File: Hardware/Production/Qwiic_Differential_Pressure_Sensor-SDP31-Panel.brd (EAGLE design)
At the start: 149.1 x 143.3 mm, 1231 parts, among them J10 QWIIC_RIGHT_ANGLE, J13 QWIIC_RIGHT_ANGLE, J14 QWIIC_RIGHT_ANGLE, J17 QWIIC_RIGHT_ANGLE, J18 QWIIC_RIGHT_ANGLE, J2 QWIIC_RIGHT_ANGLE, J21 QWIIC_RIGHT_ANGLE, J22 QWIIC_RIGHT_ANGLE, J25 QWIIC_RIGHT_ANGLE, J26 QWIIC_RIGHT_ANGLE, J29 QWIIC_RIGHT_ANGLE, J30 QWIIC_RIGHT_ANGLE, J33 QWIIC_RIGHT_ANGLE, J34 QWIIC_RIGHT_ANGLE, J37 QWIIC_RIGHT_ANGLE, J38 QWIIC_RIGHT_ANGLE, J4 QWIIC_RIGHT_ANGLE, J41 QWIIC_RIGHT_ANGLE, J42 QWIIC_RIGHT_ANGLE, J45 QWIIC_RIGHT_ANGLE, J46 QWIIC_RIGHT_ANGLE, J49 QWIIC_RIGHT_ANGLE, J5 QWIIC_RIGHT_ANGLE, J50 QWIIC_RIGHT_ANGLE, J53 QWIIC_RIGHT_ANGLE, J54 QWIIC_RIGHT_ANGLE, J57 QWIIC_RIGHT_ANGLE, J58 QWIIC_RIGHT_ANGLE, J6 QWIIC_RIGHT_ANGLE, J61 QWIIC_RIGHT_ANGLE, J62 QWIIC_RIGHT_ANGLE, J65 QWIIC_RIGHT_ANGLE, J66 QWIIC_RIGHT_ANGLE, J69 QWIIC_RIGHT_ANGLE, J70 QWIIC_RIGHT_ANGLE, J73 QWIIC_RIGHT_ANGLE, J74 QWIIC_RIGHT_ANGLE, J77 QWIIC_RIGHT_ANGLE, J78 QWIIC_RIGHT_ANGLE, J81 QWIIC_RIGHT_ANGLE, J82 QWIIC_RIGHT_ANGLE, J85 QWIIC_RIGHT_ANGLE, J86 QWIIC_RIGHT_ANGLE, J89 QWIIC_RIGHT_ANGLE, J9 QWIIC_RIGHT_ANGLE, J90 QWIIC_RIGHT_ANGLE, J93 QWIIC_RIGHT_ANGLE, J94 QWIIC_RIGHT_ANGLE, J97 QWIIC_RIGHT_ANGLE, J98 QWIIC_RIGHT_ANGLE, U1 SDP31, U10 SDP31, U11 SDP31, U12 SDP31, U13 SDP31, U14 SDP31, U15 SDP31, U16 SDP31, U17 SDP31, U18 SDP31, U19 SDP31, U2 SDP31, U20 SDP31, U21 SDP31, U22 SDP31, U23 SDP31, U24 SDP31, U25 SDP31, U3 SDP31, U4 SDP31, U5 SDP31, U6 SDP31, U7 SDP31, U8 SDP31, U9 SDP31

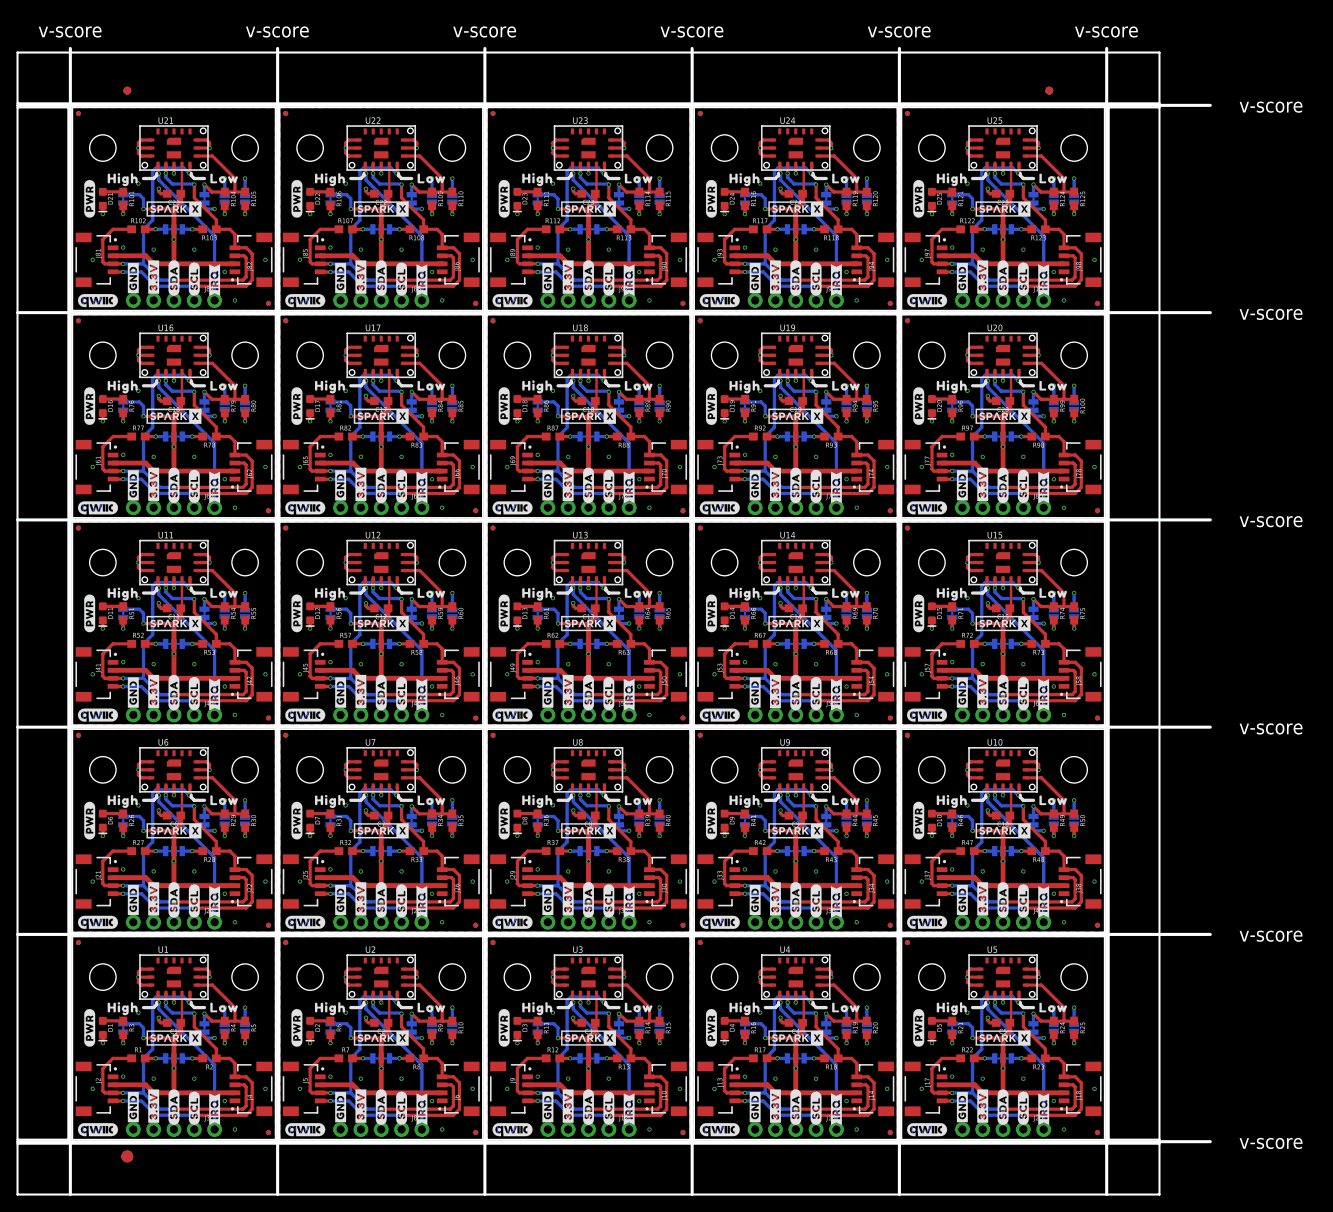
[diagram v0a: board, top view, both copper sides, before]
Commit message: Change IRQ to INT. Add Address label.
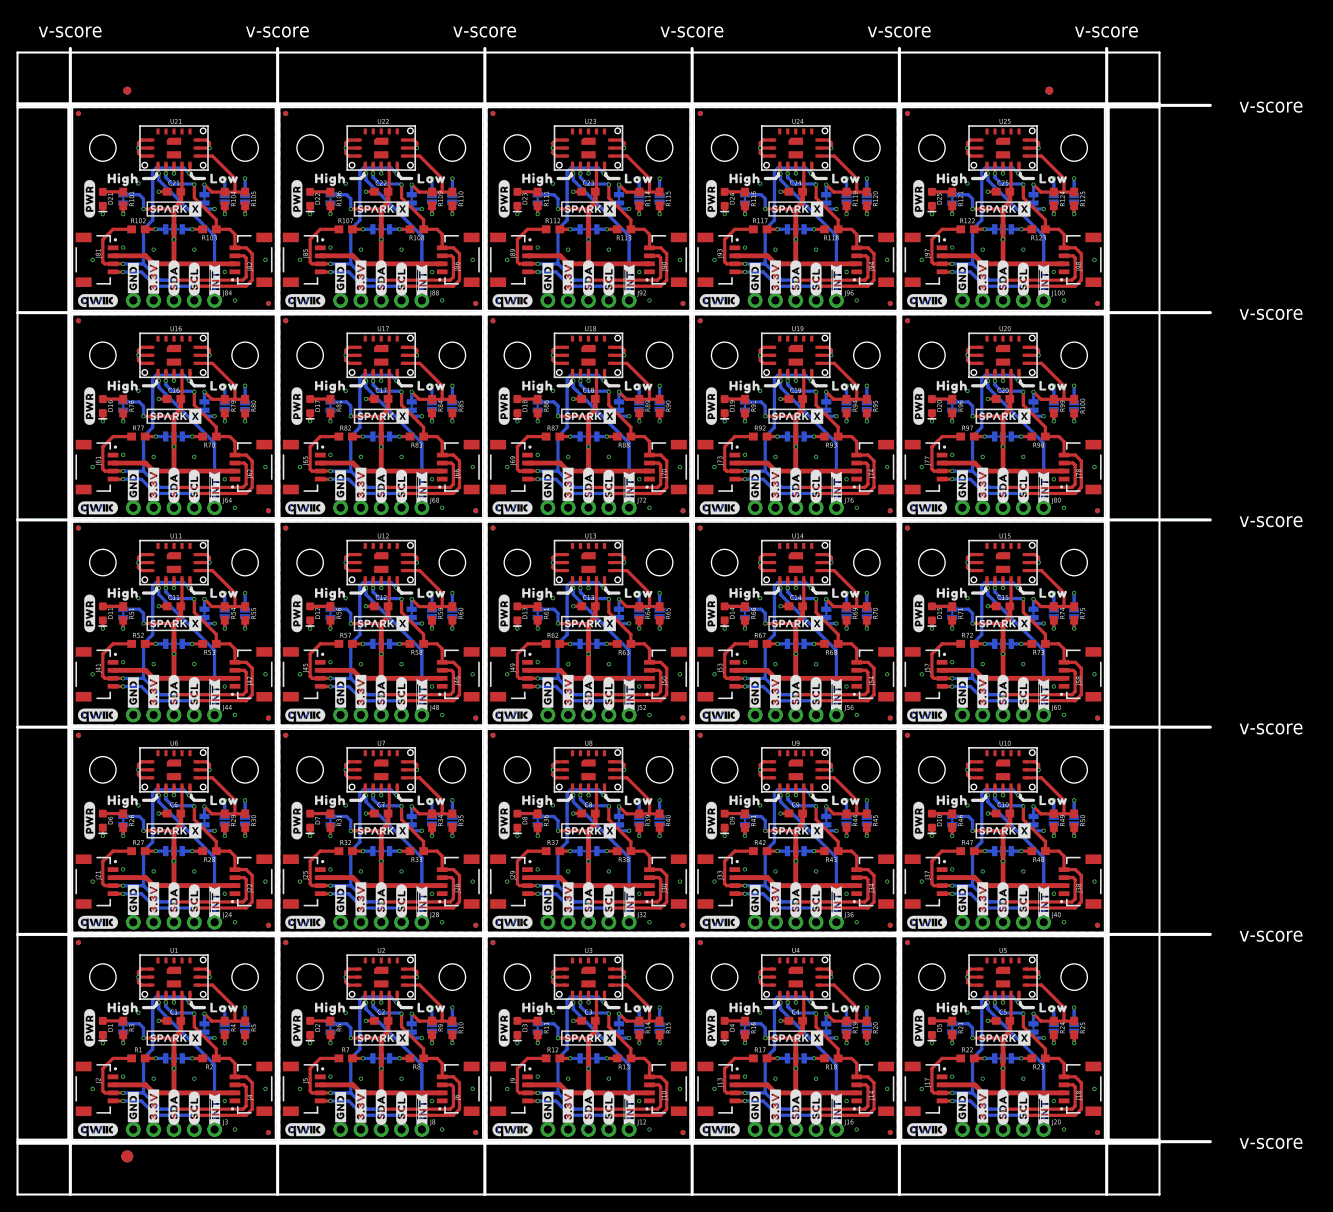
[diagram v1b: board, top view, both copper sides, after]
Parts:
- added U$626: (no value), SparkFun-Aesthetics:QWIIC_5MM
- added U$627, U$647: SPARKX-LOGO3, SparkX:SPARKX-SMALL
- added U$628: (no value), output:#PWR#0
- added U$629, U$633: (no value), output:#GND#0
- added U$630, U$634: (no value), output:#3#3V#0
- added U$631, U$635: (no value), output:#SDA#0
- added U$632, U$636: (no value), output:#SCL#0
- added U$637: (no value), output:#0X21#0
- added U$638: (no value), output:#0X22#0
- added U$639: (no value), output:#0X23#0
- added U$640: (no value), output:DIFFERENTIAL0
- added U$641: (no value), output:PRESSURE0
- added U$642: (no value), output:SENSOR0
- added U$643: (no value), output:SDP310
- added U$644: (no value), output:#LED#0
- added U$645: (no value), output:HIGH0
- added U$646: (no value), output:LOW0
- added U$648, U$649: (no value), output:##INT##0
- added U$650: (no value), output:#ADDRESS#0
- U$100, U$178: value SPARKX-LOGO3 -> (none); device SparkX:SPARKX-SMALL -> output:LOW0
- U$101, U$601: value (none) -> SPARKX-LOGO3; device SparkFun-Buzzard:I2C -> SparkX:SPARKX-SMALL
- U$102, U$77: device SparkFun-Aesthetics:QWIIC_5MM -> output:##INT##0
- U$103, U$128, U$50: value SPARKX-LOGO3 -> (none); device SparkX:SPARKX-SMALL -> output:##INT##0
- U$104: device output:#PWR#0 -> output:#ADDRESS#0
- U$105, U$209: device output:#GND#0 -> SparkFun-Buzzard:I2C
- U$106, U$210: device output:#3#3V#0 -> SparkFun-Aesthetics:QWIIC_5MM
- U$107, U$211, U$257, U$361: value (none) -> SPARKX-LOGO3; device output:#SDA#0 -> SparkX:SPARKX-SMALL
- U$108, U$212: device output:#SCL#0 -> output:#PWR#0
- U$113, U$139, U$213, U$239: device output:#IRQ#0 -> output:#GND#0
- U$114, U$188, U$214, U$88: device output:#IRQ#0 -> output:#3#3V#0
- U$115, U$215: device output:#0X21#0 -> output:#SDA#0
- U$116, U$216: device output:#0X22#0 -> output:#SCL#0
- U$117: device output:#0X23#0 -> output:#0X21#0
- U$118: device output:DIFFERENTIAL0 -> output:#0X22#0
- U$119: device output:PRESSURE0 -> output:#0X23#0
- U$120: device output:SENSOR0 -> output:DIFFERENTIAL0
- U$121: device output:SDP310 -> output:PRESSURE0
- U$122: device output:#LED#0 -> output:SENSOR0
- U$123: device output:HIGH0 -> output:SDP310
- U$124: device output:LOW0 -> output:#LED#0
- U$125, U$203: value SPARKX-LOGO3 -> (none); device SparkX:SPARKX-SMALL -> output:HIGH0
- U$126: device SparkFun-Buzzard:I2C -> output:LOW0
- U$127: value (none) -> SPARKX-LOGO3; device SparkFun-Aesthetics:QWIIC_5MM -> SparkX:SPARKX-SMALL
- U$129, U$154: device output:#PWR#0 -> output:##INT##0
- U$130, U$234: device output:#GND#0 -> output:#ADDRESS#0
- U$131, U$235: device output:#3#3V#0 -> SparkFun-Buzzard:I2C
- U$132, U$236: device output:#SDA#0 -> SparkFun-Aesthetics:QWIIC_5MM
- U$133, U$237, U$283, U$387: value (none) -> SPARKX-LOGO3; device output:#SCL#0 -> SparkX:SPARKX-SMALL
- U$134, U$25: device output:#GND#0 -> output:#PWR#0
- U$135, U$26, U$30, U$581: device output:#3#3V#0 -> output:#GND#0
- U$136, U$27, U$31, U$582: device output:#SDA#0 -> output:#3#3V#0
- U$137, U$28, U$37, U$583: device output:#SCL#0 -> output:#SDA#0
- U$138, U$164, U$38, U$64: device output:#IRQ#0 -> output:#SCL#0
- U$140, U$240: device output:#0X21#0 -> output:#3#3V#0
- U$141, U$241: device output:#0X22#0 -> output:#SDA#0
- U$142, U$242: device output:#0X23#0 -> output:#SCL#0
- U$143: device output:DIFFERENTIAL0 -> output:#0X21#0
- U$144: device output:PRESSURE0 -> output:#0X22#0
- U$145: device output:SENSOR0 -> output:#0X23#0
- U$146: device output:SDP310 -> output:DIFFERENTIAL0
- U$147: device output:#LED#0 -> output:PRESSURE0
- U$148: device output:HIGH0 -> output:SENSOR0
- U$149: device output:LOW0 -> output:SDP310
- U$150, U$228: value SPARKX-LOGO3 -> (none); device SparkX:SPARKX-SMALL -> output:#LED#0
- U$151: device SparkFun-Buzzard:I2C -> output:HIGH0
- U$152: device SparkFun-Aesthetics:QWIIC_5MM -> output:LOW0
- U$155, U$180, U$259, U$284: device output:#GND#0 -> output:##INT##0
- U$156, U$260: device output:#3#3V#0 -> output:#ADDRESS#0
- U$157, U$261: device output:#SDA#0 -> SparkFun-Buzzard:I2C
- U$158, U$262: device output:#SCL#0 -> SparkFun-Aesthetics:QWIIC_5MM
- U$159, U$205, U$309, U$55: value (none) -> SPARKX-LOGO3; device output:#GND#0 -> SparkX:SPARKX-SMALL
- U$160, U$56: device output:#3#3V#0 -> output:#PWR#0
- U$161, U$57, U$607, U$61: device output:#SDA#0 -> output:#GND#0
- U$162, U$58, U$608, U$62: device output:#SCL#0 -> output:#3#3V#0
- U$163, U$189, U$63, U$89: device output:#IRQ#0 -> output:#SDA#0
- U$165, U$265: device output:#0X21#0 -> output:#GND#0
- U$166, U$266: device output:#0X22#0 -> output:#3#3V#0
- U$167, U$267: device output:#0X23#0 -> output:#SDA#0
- U$168, U$268: device output:DIFFERENTIAL0 -> output:#SCL#0
- U$169: device output:PRESSURE0 -> output:#0X21#0
- U$170: device output:SENSOR0 -> output:#0X22#0
- U$171: device output:SDP310 -> output:#0X23#0
- U$172: device output:#LED#0 -> output:DIFFERENTIAL0
- U$173: device output:HIGH0 -> output:PRESSURE0
- U$174: device output:LOW0 -> output:SENSOR0
- U$175, U$253: value SPARKX-LOGO3 -> (none); device SparkX:SPARKX-SMALL -> output:SDP310
- U$176: device SparkFun-Buzzard:I2C -> output:#LED#0
- U$177: device SparkFun-Aesthetics:QWIIC_5MM -> output:HIGH0
- U$179, U$24: value (none) -> SPARKX-LOGO3; device output:#PWR#0 -> SparkX:SPARKX-SMALL
- U$181, U$206, U$285, U$310: device output:#3#3V#0 -> output:##INT##0
- U$182, U$286: device output:#SDA#0 -> output:#ADDRESS#0
- U$183, U$287: device output:#SCL#0 -> SparkFun-Buzzard:I2C
- U$184, U$80: device output:#GND#0 -> SparkFun-Aesthetics:QWIIC_5MM
- U$185, U$231, U$335, U$81: value (none) -> SPARKX-LOGO3; device output:#3#3V#0 -> SparkX:SPARKX-SMALL
- U$186, U$82: device output:#SDA#0 -> output:#PWR#0
- U$187, U$83, U$87: device output:#SCL#0 -> output:#GND#0
- U$190, U$90: device output:#0X21#0 -> output:#SCL#0
- U$191, U$291: device output:#0X22#0 -> output:#GND#0
- U$192, U$292: device output:#0X23#0 -> output:#3#3V#0
- U$193, U$293: device output:DIFFERENTIAL0 -> output:#SDA#0
- U$194, U$294: device output:PRESSURE0 -> output:#SCL#0
- U$195: device output:SENSOR0 -> output:#0X21#0
- U$196: device output:SDP310 -> output:#0X22#0
- U$197: device output:#LED#0 -> output:#0X23#0
- U$198: device output:HIGH0 -> output:DIFFERENTIAL0
- U$199: device output:LOW0 -> output:PRESSURE0
- U$200, U$278: value SPARKX-LOGO3 -> (none); device SparkX:SPARKX-SMALL -> output:SENSOR0
- U$201: device SparkFun-Buzzard:I2C -> output:SDP310
- U$202: device SparkFun-Aesthetics:QWIIC_5MM -> output:#LED#0
- U$204: device output:#PWR#0 -> output:LOW0
- U$207, U$232, U$311, U$336: device output:#SDA#0 -> output:##INT##0
- U$208, U$312: device output:#SCL#0 -> output:#ADDRESS#0
- U$21: device SparkFun-Buzzard:I2C -> output:#ADDRESS#0
- U$217, U$317: device output:#0X23#0 -> output:#GND#0
- U$218, U$318: device output:DIFFERENTIAL0 -> output:#3#3V#0
- U$219, U$319: device output:PRESSURE0 -> output:#SDA#0
- U$22: device SparkFun-Aesthetics:QWIIC_5MM -> SparkFun-Buzzard:I2C
- U$220, U$320: device output:SENSOR0 -> output:#SCL#0
- U$221: device output:SDP310 -> output:#0X21#0
- U$222: device output:#LED#0 -> output:#0X22#0
- U$223: device output:HIGH0 -> output:#0X23#0
- U$224: device output:LOW0 -> output:DIFFERENTIAL0
- U$225, U$303: value SPARKX-LOGO3 -> (none); device SparkX:SPARKX-SMALL -> output:PRESSURE0
- U$226: device SparkFun-Buzzard:I2C -> output:SENSOR0
- U$227: device SparkFun-Aesthetics:QWIIC_5MM -> output:SDP310
- U$229: device output:#PWR#0 -> output:HIGH0
- U$23, U$600: value SPARKX-LOGO3 -> (none); device SparkX:SPARKX-SMALL -> SparkFun-Aesthetics:QWIIC_5MM
- U$230, U$334: device output:#GND#0 -> output:LOW0
- U$233, U$258, U$337, U$362: device output:#SCL#0 -> output:##INT##0
- U$238, U$264: device output:#IRQ#0 -> output:#PWR#0
- U$243, U$343: device output:DIFFERENTIAL0 -> output:#GND#0
- U$244, U$344: device output:PRESSURE0 -> output:#3#3V#0
- U$245, U$345: device output:SENSOR0 -> output:#SDA#0
- U$246, U$346: device output:SDP310 -> output:#SCL#0
- U$247: device output:#LED#0 -> output:#0X21#0
- U$248: device output:HIGH0 -> output:#0X22#0
- U$249: device output:LOW0 -> output:#0X23#0
- U$250, U$328: value SPARKX-LOGO3 -> (none); device SparkX:SPARKX-SMALL -> output:DIFFERENTIAL0
- U$251: device SparkFun-Buzzard:I2C -> output:PRESSURE0
- U$252: device SparkFun-Aesthetics:QWIIC_5MM -> output:SENSOR0
- U$254: device output:#PWR#0 -> output:#LED#0
- U$255, U$359: device output:#GND#0 -> output:HIGH0
- U$256, U$360: device output:#3#3V#0 -> output:LOW0
- U$263, U$289, U$413, U$439: value (none) -> SPARKX-LOGO3; device output:#IRQ#0 -> SparkX:SPARKX-SMALL
- U$269, U$369: device output:PRESSURE0 -> output:#GND#0
- U$270, U$370: device output:SENSOR0 -> output:#3#3V#0
- U$271, U$371: device output:SDP310 -> output:#SDA#0
- U$272, U$372: device output:#LED#0 -> output:#SCL#0
- U$273: device output:HIGH0 -> output:#0X21#0
- U$274: device output:LOW0 -> output:#0X22#0
- U$275, U$353: value SPARKX-LOGO3 -> (none); device SparkX:SPARKX-SMALL -> output:#0X23#0
- U$276: device SparkFun-Buzzard:I2C -> output:DIFFERENTIAL0
- U$277: device SparkFun-Aesthetics:QWIIC_5MM -> output:PRESSURE0
- U$279: device output:#PWR#0 -> output:SDP310
- U$280, U$384: device output:#GND#0 -> output:#LED#0
- U$281, U$385: device output:#3#3V#0 -> output:HIGH0
- U$282, U$386: device output:#SDA#0 -> output:LOW0
- U$288, U$314: device output:#IRQ#0 -> SparkFun-Aesthetics:QWIIC_5MM
- U$29, U$480, U$580, U$584: device output:#GND#0 -> output:#SCL#0
- U$290: device output:#0X21#0 -> output:#PWR#0
- U$295, U$395: device output:SENSOR0 -> output:#GND#0
- U$296, U$396: device output:SDP310 -> output:#3#3V#0
- U$297, U$397: device output:#LED#0 -> output:#SDA#0
- U$298, U$398: device output:HIGH0 -> output:#SCL#0
- U$299: device output:LOW0 -> output:#0X21#0
- U$300, U$378: value SPARKX-LOGO3 -> (none); device SparkX:SPARKX-SMALL -> output:#0X22#0
- U$301: device SparkFun-Buzzard:I2C -> output:#0X23#0
- U$302: device SparkFun-Aesthetics:QWIIC_5MM -> output:DIFFERENTIAL0
- U$304: device output:#PWR#0 -> output:SENSOR0
- U$305, U$409: device output:#GND#0 -> output:SDP310
- U$306, U$410: device output:#3#3V#0 -> output:#LED#0
- U$307, U$411: device output:#SDA#0 -> output:HIGH0
- U$308, U$412: device output:#SCL#0 -> output:LOW0
- U$313, U$339: device output:#IRQ#0 -> SparkFun-Buzzard:I2C
- U$315, U$465: value (none) -> SPARKX-LOGO3; device output:#0X21#0 -> SparkX:SPARKX-SMALL
- U$316: device output:#0X22#0 -> output:#PWR#0
- U$321, U$421: device output:SDP310 -> output:#GND#0
- U$322, U$422: device output:#LED#0 -> output:#3#3V#0
- U$323, U$423: device output:HIGH0 -> output:#SDA#0
- U$324, U$424: device output:LOW0 -> output:#SCL#0
- U$325, U$403: value SPARKX-LOGO3 -> (none); device SparkX:SPARKX-SMALL -> output:#0X21#0
- U$326: device SparkFun-Buzzard:I2C -> output:#0X22#0
- U$327: device SparkFun-Aesthetics:QWIIC_5MM -> output:#0X23#0
- U$329: device output:#PWR#0 -> output:PRESSURE0
- U$330, U$434: device output:#GND#0 -> output:SENSOR0
- U$331, U$435: device output:#3#3V#0 -> output:SDP310
- U$332, U$436: device output:#SDA#0 -> output:#LED#0
- U$333, U$437: device output:#SCL#0 -> output:HIGH0
- U$338, U$364: device output:#IRQ#0 -> output:#ADDRESS#0
- U$340: device output:#0X21#0 -> SparkFun-Aesthetics:QWIIC_5MM
- U$341, U$491: value (none) -> SPARKX-LOGO3; device output:#0X22#0 -> SparkX:SPARKX-SMALL
- U$342: device output:#0X23#0 -> output:#PWR#0
- U$347, U$447: device output:#LED#0 -> output:#GND#0
- U$348, U$448: device output:HIGH0 -> output:#3#3V#0
- U$349, U$449: device output:LOW0 -> output:#SDA#0
- U$350, U$428, U$450, U$528: value SPARKX-LOGO3 -> (none); device SparkX:SPARKX-SMALL -> output:#SCL#0
- U$351: device SparkFun-Buzzard:I2C -> output:#0X21#0
- U$352: device SparkFun-Aesthetics:QWIIC_5MM -> output:#0X22#0
- U$354: device output:#PWR#0 -> output:DIFFERENTIAL0
- U$355, U$459: device output:#GND#0 -> output:PRESSURE0
- U$356, U$460: device output:#3#3V#0 -> output:SENSOR0
- U$357, U$461: device output:#SDA#0 -> output:SDP310
- U$358, U$462: device output:#SCL#0 -> output:#LED#0
- U$363, U$388, U$389, U$414, U$5, U$6: device output:#IRQ#0 -> output:##INT##0
- U$365: device output:#0X21#0 -> SparkFun-Buzzard:I2C
- U$366: device output:#0X22#0 -> SparkFun-Aesthetics:QWIIC_5MM
- U$367, U$517: value (none) -> SPARKX-LOGO3; device output:#0X23#0 -> SparkX:SPARKX-SMALL
- U$368: device output:DIFFERENTIAL0 -> output:#PWR#0
- U$373, U$473: device output:HIGH0 -> output:#GND#0
- U$374, U$474: device output:LOW0 -> output:#3#3V#0
- U$375, U$453, U$475, U$553: value SPARKX-LOGO3 -> (none); device SparkX:SPARKX-SMALL -> output:#SDA#0
- U$376, U$476: device SparkFun-Buzzard:I2C -> output:#SCL#0
- U$377: device SparkFun-Aesthetics:QWIIC_5MM -> output:#0X21#0
- U$379: device output:#PWR#0 -> output:#0X23#0
- U$380, U$484: device output:#GND#0 -> output:DIFFERENTIAL0
- U$381, U$485: device output:#3#3V#0 -> output:PRESSURE0
- U$382, U$486: device output:#SDA#0 -> output:SENSOR0
- U$383, U$487: device output:#SCL#0 -> output:SDP310
- U$39: device output:#IRQ#0 -> output:#0X21#0
- U$390: device output:#0X21#0 -> output:#ADDRESS#0
- U$391: device output:#0X22#0 -> SparkFun-Buzzard:I2C
- U$392: device output:#0X23#0 -> SparkFun-Aesthetics:QWIIC_5MM
- U$393, U$543: value (none) -> SPARKX-LOGO3; device output:DIFFERENTIAL0 -> SparkX:SPARKX-SMALL
- U$394: device output:PRESSURE0 -> output:#PWR#0
- U$399, U$499: device output:LOW0 -> output:#GND#0
- U$40: device output:#0X21#0 -> output:#0X22#0
- U$400, U$478, U$500, U$578: value SPARKX-LOGO3 -> (none); device SparkX:SPARKX-SMALL -> output:#3#3V#0
- U$401, U$501: device SparkFun-Buzzard:I2C -> output:#SDA#0
- U$402, U$502: device SparkFun-Aesthetics:QWIIC_5MM -> output:#SCL#0
- U$404: device output:#PWR#0 -> output:#0X22#0
- U$405, U$509: device output:#GND#0 -> output:#0X23#0
- U$406, U$510: device output:#3#3V#0 -> output:DIFFERENTIAL0
- U$407, U$511: device output:#SDA#0 -> output:PRESSURE0
- U$408, U$512: device output:#SCL#0 -> output:SENSOR0
- U$41: device output:#0X22#0 -> output:#0X23#0
- U$415, U$440: device output:#0X21#0 -> output:##INT##0
- U$416: device output:#0X22#0 -> output:#ADDRESS#0
- U$417: device output:#0X23#0 -> SparkFun-Buzzard:I2C
- U$418: device output:DIFFERENTIAL0 -> SparkFun-Aesthetics:QWIIC_5MM
- U$419, U$569: value (none) -> SPARKX-LOGO3; device output:PRESSURE0 -> SparkX:SPARKX-SMALL
- U$42: device output:#0X23#0 -> output:DIFFERENTIAL0
- U$420: device output:SENSOR0 -> output:#PWR#0
- U$425, U$503, U$525, U$603: value SPARKX-LOGO3 -> (none); device SparkX:SPARKX-SMALL -> output:#GND#0
- U$426, U$526: device SparkFun-Buzzard:I2C -> output:#3#3V#0
- U$427, U$527: device SparkFun-Aesthetics:QWIIC_5MM -> output:#SDA#0
- U$429: device output:#PWR#0 -> output:#0X21#0
- U$43: device output:DIFFERENTIAL0 -> output:PRESSURE0
- U$430, U$534: device output:#GND#0 -> output:#0X22#0
- U$431, U$535: device output:#3#3V#0 -> output:#0X23#0
- U$432, U$536: device output:#SDA#0 -> output:DIFFERENTIAL0
- U$433, U$537: device output:#SCL#0 -> output:PRESSURE0
- U$438, U$464: device output:#IRQ#0 -> output:LOW0
- U$44: device output:PRESSURE0 -> output:SENSOR0
- U$441, U$466: device output:#0X22#0 -> output:##INT##0
- U$442: device output:#0X23#0 -> output:#ADDRESS#0
- U$443: device output:DIFFERENTIAL0 -> SparkFun-Buzzard:I2C
- U$444: device output:PRESSURE0 -> SparkFun-Aesthetics:QWIIC_5MM
- U$445, U$595: value (none) -> SPARKX-LOGO3; device output:SENSOR0 -> SparkX:SPARKX-SMALL
- U$446: device output:SDP310 -> output:#PWR#0
- U$45: device output:SENSOR0 -> output:SDP310
- U$451, U$551: device SparkFun-Buzzard:I2C -> output:#GND#0
- U$452, U$552: device SparkFun-Aesthetics:QWIIC_5MM -> output:#3#3V#0
- U$454, U$554: device output:#PWR#0 -> output:#SCL#0
- U$455, U$559: device output:#GND#0 -> output:#0X21#0
- U$456, U$560: device output:#3#3V#0 -> output:#0X22#0
- U$457, U$561: device output:#SDA#0 -> output:#0X23#0
- U$458, U$562: device output:#SCL#0 -> output:DIFFERENTIAL0
- U$46: device output:SDP310 -> output:#LED#0
- U$463, U$489: device output:#IRQ#0 -> output:HIGH0
- U$467, U$492: device output:#0X23#0 -> output:##INT##0
- U$468: device output:DIFFERENTIAL0 -> output:#ADDRESS#0
- U$469: device output:PRESSURE0 -> SparkFun-Buzzard:I2C
- U$47: device output:#LED#0 -> output:HIGH0
- U$470: device output:SENSOR0 -> SparkFun-Aesthetics:QWIIC_5MM
- U$471, U$621: value (none) -> SPARKX-LOGO3; device output:SDP310 -> SparkX:SPARKX-SMALL
- U$472: device output:#LED#0 -> output:#PWR#0
- U$477, U$577: device SparkFun-Aesthetics:QWIIC_5MM -> output:#GND#0
- U$479, U$579: device output:#PWR#0 -> output:#SDA#0
- U$48: device output:HIGH0 -> output:LOW0
- U$481, U$585: device output:#3#3V#0 -> output:#0X21#0
- U$482, U$586: device output:#SDA#0 -> output:#0X22#0
- U$483, U$587: device output:#SCL#0 -> output:#0X23#0
- U$488, U$514: device output:#IRQ#0 -> output:#LED#0
- U$49, U$549: value (none) -> SPARKX-LOGO3; device output:LOW0 -> SparkX:SPARKX-SMALL
- U$490: device output:#0X21#0 -> output:LOW0
- U$493, U$518: device output:DIFFERENTIAL0 -> output:##INT##0
- U$494: device output:PRESSURE0 -> output:#ADDRESS#0
- U$495: device output:SENSOR0 -> SparkFun-Buzzard:I2C
- U$496: device output:SDP310 -> SparkFun-Aesthetics:QWIIC_5MM
- U$497: value (none) -> SPARKX-LOGO3; device output:#LED#0 -> SparkX:SPARKX-SMALL
- U$498: device output:HIGH0 -> output:#PWR#0
- U$504, U$604: device output:#PWR#0 -> output:#3#3V#0
- U$505, U$59, U$605, U$609: device output:#GND#0 -> output:#SDA#0
- U$506, U$60, U$606, U$610: device output:#3#3V#0 -> output:#SCL#0
- U$507, U$611: device output:#SDA#0 -> output:#0X21#0
- U$508, U$612: device output:#SCL#0 -> output:#0X22#0
- U$51, U$76: device SparkFun-Buzzard:I2C -> output:##INT##0
- U$513, U$539: device output:#IRQ#0 -> output:SDP310
- U$515: device output:#0X21#0 -> output:HIGH0
- U$516: device output:#0X22#0 -> output:LOW0
- U$519, U$544: device output:PRESSURE0 -> output:##INT##0
- U$52: device SparkFun-Aesthetics:QWIIC_5MM -> output:#ADDRESS#0
- U$520: device output:SENSOR0 -> output:#ADDRESS#0
- U$521: device output:SDP310 -> SparkFun-Buzzard:I2C
- U$522: device output:#LED#0 -> SparkFun-Aesthetics:QWIIC_5MM
- U$523: value (none) -> SPARKX-LOGO3; device output:HIGH0 -> SparkX:SPARKX-SMALL
- U$524: device output:LOW0 -> output:#PWR#0
- U$529: device output:#PWR#0 -> output:#GND#0
- U$53, U$625: value SPARKX-LOGO3 -> (none); device SparkX:SPARKX-SMALL -> SparkFun-Buzzard:I2C
- U$530, U$84: device output:#GND#0 -> output:#3#3V#0
- U$531, U$85: device output:#3#3V#0 -> output:#SDA#0
- U$532, U$86: device output:#SDA#0 -> output:#SCL#0
- U$533: device output:#SCL#0 -> output:#0X21#0
- U$538, U$564: device output:#IRQ#0 -> output:SENSOR0
- U$54: device output:#PWR#0 -> SparkFun-Aesthetics:QWIIC_5MM
- U$540: device output:#0X21#0 -> output:#LED#0
- U$541: device output:#0X22#0 -> output:HIGH0
- U$542: device output:#0X23#0 -> output:LOW0
- U$545, U$570: device output:SENSOR0 -> output:##INT##0
- U$546: device output:SDP310 -> output:#ADDRESS#0
- U$547: device output:#LED#0 -> SparkFun-Buzzard:I2C
- U$548: device output:HIGH0 -> SparkFun-Aesthetics:QWIIC_5MM
- U$550: value SPARKX-LOGO3 -> (none); device SparkX:SPARKX-SMALL -> output:#PWR#0
- U$563, U$589: device output:#IRQ#0 -> output:PRESSURE0
- U$565: device output:#0X21#0 -> output:SDP310
- U$566: device output:#0X22#0 -> output:#LED#0
- U$567: device output:#0X23#0 -> output:HIGH0
- U$568: device output:DIFFERENTIAL0 -> output:LOW0
- U$571, U$596: device output:SDP310 -> output:##INT##0
- U$572: device output:#LED#0 -> output:#ADDRESS#0
- U$573: device output:HIGH0 -> SparkFun-Buzzard:I2C
- U$574: device output:LOW0 -> SparkFun-Aesthetics:QWIIC_5MM
- U$576: device SparkFun-Buzzard:I2C -> output:#PWR#0
- U$588, U$614: device output:#IRQ#0 -> output:DIFFERENTIAL0
- U$590: device output:#0X21#0 -> output:SENSOR0
- U$591: device output:#0X22#0 -> output:SDP310
- U$592: device output:#0X23#0 -> output:#LED#0
- U$593: device output:DIFFERENTIAL0 -> output:HIGH0
- U$594: device output:PRESSURE0 -> output:LOW0
- U$597, U$622: device output:#LED#0 -> output:##INT##0
- U$598: device output:HIGH0 -> output:#ADDRESS#0
- U$599: device output:LOW0 -> SparkFun-Buzzard:I2C
- U$602: device SparkFun-Aesthetics:QWIIC_5MM -> output:#PWR#0
- U$613: device output:#IRQ#0 -> output:#0X23#0
- U$615: device output:#0X21#0 -> output:PRESSURE0
- U$616: device output:#0X22#0 -> output:SENSOR0
- U$617: device output:#0X23#0 -> output:SDP310
- U$618: device output:DIFFERENTIAL0 -> output:#LED#0
- U$619: device output:PRESSURE0 -> output:HIGH0
- U$620: device output:SENSOR0 -> output:LOW0
- U$623: device output:HIGH0 -> output:##INT##0
- U$624: device output:LOW0 -> output:#ADDRESS#0
- U$78: value SPARKX-LOGO3 -> (none); device SparkX:SPARKX-SMALL -> output:#ADDRESS#0
- U$79: device output:#PWR#0 -> SparkFun-Buzzard:I2C
- U$91: device output:#0X22#0 -> output:#0X21#0
- U$92: device output:#0X23#0 -> output:#0X22#0
- U$93: device output:DIFFERENTIAL0 -> output:#0X23#0
- U$94: device output:PRESSURE0 -> output:DIFFERENTIAL0
- U$95: device output:SENSOR0 -> output:PRESSURE0
- U$96: device output:SDP310 -> output:SENSOR0
- U$97: device output:#LED#0 -> output:SDP310
- U$98: device output:HIGH0 -> output:#LED#0
- U$99: device output:LOW0 -> output:HIGH0
- moved U$379 126.5 mm to (125.2, 62.5), flipped to the bottom
- moved U$129 124.6 mm to (121.4, 3.81), flipped to the bottom
- moved U$128 121.3 mm to (121.4, 3.81), flipped to the top, turned to 90 degrees
- moved U$378 120.9 mm to (122.7, 62.5), turned to 90 degrees
- moved U$509 119.2 mm to (125.2, 88.4)
- moved U$377 118.1 mm to (120.1, 62.6), flipped to the bottom, turned to 90 degrees
- moved U$502 118.0 mm to (118.9, 81.7), turned to 90 degrees
- moved U$504 117.2 mm to (113.8, 81.9), flipped to the bottom
- moved U$518 117.1 mm to (121.4, 81.5), flipped to the top, turned to 90 degrees
- moved U$259 116.8 mm to (121.4, 29.7)
- moved U$519 116.6 mm to (121.4, 81.5), turned to 90 degrees
- moved U$130 115.9 mm to (122.7, 15.9), flipped to the bottom, turned to 0 degrees
- moved U$127 114.1 mm to (116.3, 12.7)
- moved U$520 113.7 mm to (122.7, 93.6)
- moved U$252 113.5 mm to (116.3, 44.7), flipped to the bottom
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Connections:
- net IRQ renamed !INT!
- net IRQ1 renamed !INT!1
- net IRQ10 renamed !INT!10
- net IRQ11 renamed !INT!11
- net IRQ12 renamed !INT!12
- net IRQ13 renamed !INT!13
- net IRQ14 renamed !INT!14
- net IRQ15 renamed !INT!15
- net IRQ16 renamed !INT!16
- net IRQ17 renamed !INT!17
- net IRQ18 renamed !INT!18
- net IRQ19 renamed !INT!19
- net IRQ2 renamed !INT!2
- net IRQ20 renamed !INT!20
- net IRQ21 renamed !INT!21
- net IRQ22 renamed !INT!22
- net IRQ23 renamed !INT!23
- net IRQ24 renamed !INT!24
- net IRQ3 renamed !INT!3
- net IRQ4 renamed !INT!4
- net IRQ5 renamed !INT!5
- net IRQ6 renamed !INT!6
- net IRQ7 renamed !INT!7
- net IRQ8 renamed !INT!8
- net IRQ9 renamed !INT!9

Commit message: Update PROD_IDs. Delete New-Parts
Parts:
- JP1, JP102, JP103, JP104, JP105, JP111, JP112, JP113, JP114, JP12, JP120, JP121, JP122, JP123, JP129, JP13, JP130, JP131, JP132, JP138, JP139, JP14, JP140, JP141, JP147, JP148, JP149, JP15, JP150, JP156, JP157, JP158, JP159, JP165, JP166, JP167, JP168, JP174, JP175, JP176, JP177, JP183, JP184, JP185, JP186, JP192, JP193, JP194, JP195, JP2, JP201, JP202, JP203, JP204, JP21, JP210, JP211, JP212, JP213, JP219, JP22, JP220, JP221, JP222, JP23, JP24, JP30, JP31, JP32, JP33, JP39, JP40, JP41, JP42, JP48, JP49, JP5, JP50, JP51, JP57, JP58, JP59, JP6, JP60, JP66, JP67, JP68, JP69, JP75, JP76, JP77, JP78, JP84, JP85, JP86, JP87, JP93, JP94, JP95, JP96: device SparkFun:MICRO-FIDUCIAL -> SparkFun-Aesthetics:FIDUCIAL-MICRO
- JP10, JP100, JP101, JP109, JP11, JP110, JP118, JP119, JP127, JP128, JP136, JP137, JP145, JP146, JP154, JP155, JP163, JP164, JP172, JP173, JP181, JP182, JP19, JP190, JP191, JP199, JP20, JP200, JP208, JP209, JP217, JP218, JP28, JP29, JP3, JP37, JP38, JP4, JP46, JP47, JP55, JP56, JP64, JP65, JP73, JP74, JP82, JP83, JP91, JP92: device SparkFun:STAND-OFF -> SparkFun-Hardware:STAND-OFF
- R10, R100, R105, R110, R115, R120, R125, R15, R20, R25, R30, R35, R40, R45, R5, R50, R55, R60, R65, R70, R75, R80, R85, R90, R95: value 2.7K -> 2.7k; device New-Parts_SparkFun-Resistors:0603 -> SparkFun-Resistors:0603
- R104, R109, R114, R119, R124, R14, R19, R24, R29, R34, R39, R4, R44, R49, R54, R59, R64, R69, R74, R79, R84, R89, R9, R94, R99: value 1.2K -> 1.20k; device New-Parts_SparkFun-Resistors:0603 -> SparkFun-Resistors:0603
- U1, U10, U11, U12, U13, U14, U15, U16, U17, U18, U19, U2, U20, U21, U22, U23, U24, U25, U3, U4, U5, U6, U7, U8, U9: device New-Parts_SparkFun-Sensors:SDP31 -> SparkFun-Sensors:SDP3X
